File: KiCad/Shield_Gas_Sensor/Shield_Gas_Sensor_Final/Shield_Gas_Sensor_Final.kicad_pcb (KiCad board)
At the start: 2 copper layers, 68.6 x 53.3 mm, 20 parts, among them P1 Power, P2 Analog, P3 Digital, P4 Digital, P5 CONN_01X01, P6 CONN_01X01, P7 CONN_01X01, P8 CONN_01X01, U1 LTC1050ACN8#PBF, U2 Gas_Sensor_TO-5, U3 RN2483_Breakout

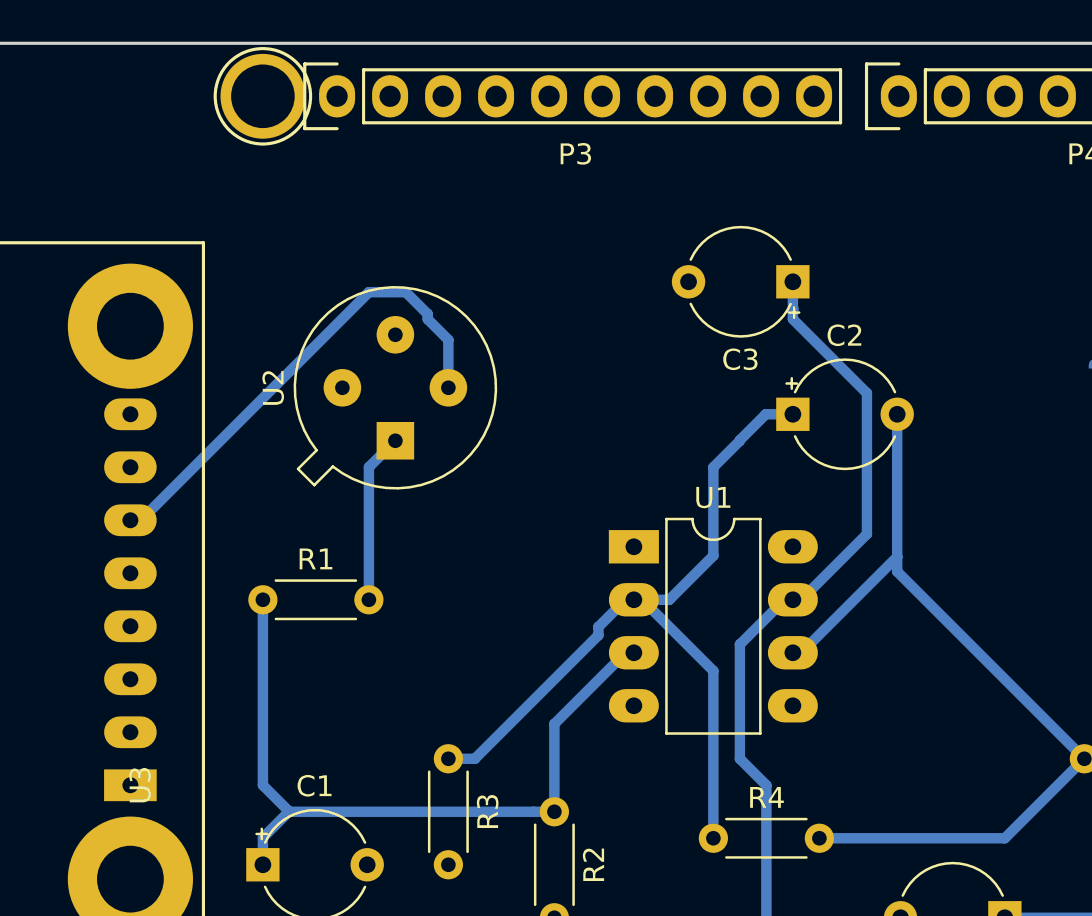
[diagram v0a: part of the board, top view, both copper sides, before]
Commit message: Correction Tx/Rx and Screens
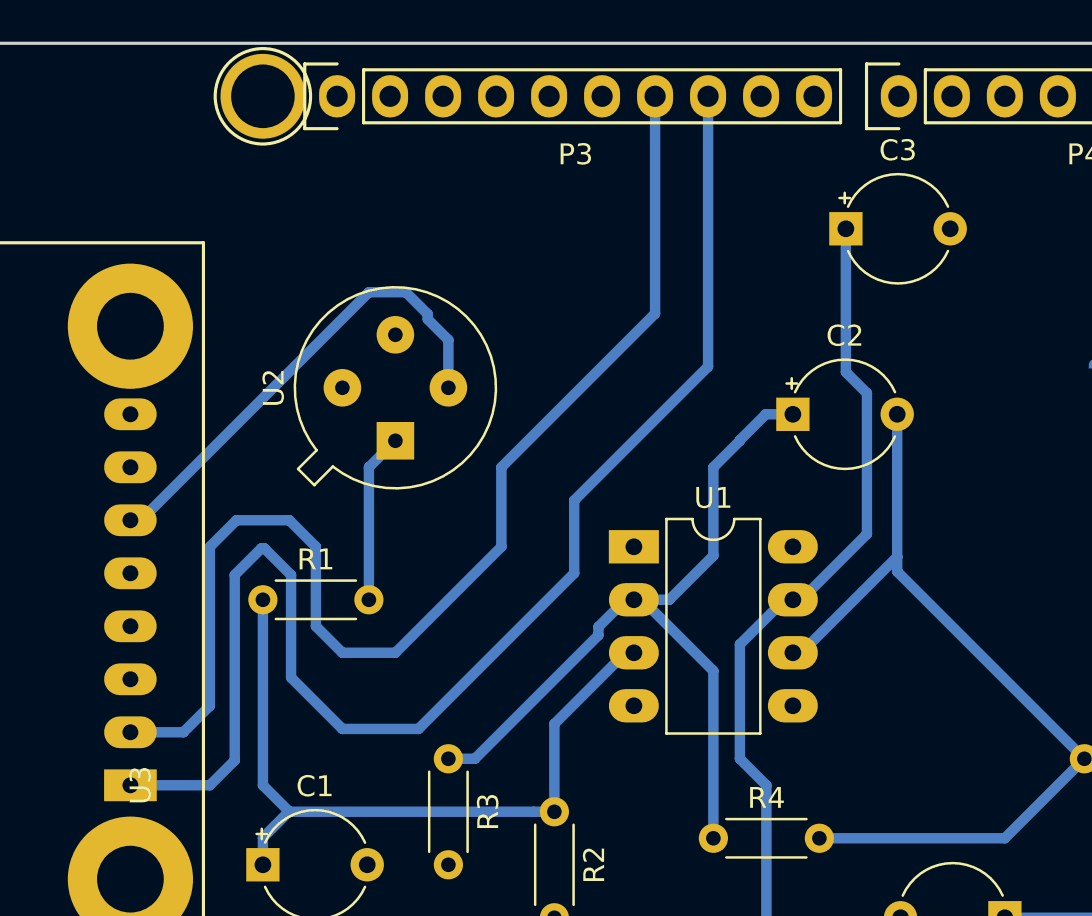
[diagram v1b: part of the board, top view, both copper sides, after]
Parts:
- moved C3 3.59 mm to (154.2, 81.9), turned to 0 degrees
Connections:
- U3 pad 1: /10 -> /10(**/SS)
- U3 pad 2: /11 -> /11(**/MOSI)
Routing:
- net /10(**/SS): track 0.00 -> 66.3 mm
- net /11(**/MOSI): track 0.00 -> 58.1 mm
- net +5V: track 44.9 -> 46.4 mm
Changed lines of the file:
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@@
     (thickness 1.6)
     (drawings 28)
-    (tracks 59)
+    (tracks 83)
     (zones 0)
     (modules 20)
-    (nets 49)
+    (nets 47)
   )
   (page A4)
@@
   (net 41 "Net-(U2-Pad3)")
   (net 42 "Net-(U2-Pad4)")
-  (net 43 /10)
-  (net 44 /11)
-  (net 45 "Net-(U3-Pad3)")
-  (net 46 "Net-(U3-Pad4)")
-  (net 47 "Net-(U3-Pad5)")
-  (net 48 "Net-(U3-Pad7)")
+  (net 43 "Net-(U3-Pad3)")
+  (net 44 "Net-(U3-Pad4)")
+  (net 45 "Net-(U3-Pad5)")
+  (net 46 "Net-(U3-Pad7)")
   (net_class Default "This is the default net class."
     (clearance 0.4)
@@
     (add_net "/0(Rx)")
     (add_net "/1(Tx)")
-    (add_net /10)
     (add_net "/10(**/SS)")
-    (add_net /11)
     (add_net "/11(**/MOSI)")
     (add_net "/12(MISO)")
@@
   )
   (module Capacitor_THT:CP_Radial_Tantal_D5.0mm_P5.00mm (layer F.Cu)
-    (at 151.638 84.455 180)
+    (at 154.178 81.915)
     (descr "CP, Radial_Tantal series, Radial, pin pitch=5.00mm, , diameter=5.0mm, Tantal Electrolytic Capacitor, http://cdn-reichelt.de/documents/datenblatt/B300/TANTAL-TB-Serie%23.pdf")
     (tags "CP Radial_Tantal series Radial pin pitch 5.00mm  diameter 5.0mm Tantal Electrolytic Capacitor")
-    (fp_text reference C3 (at 2.5 -3.75 180) (layer F.SilkS)
-      (effects (font (size 1 1) (thickness 0.15)))
-    )
-    (fp_text value 100n (at 2.5 3.75 180) (layer F.Fab)
-      (effects (font (size 1 1) (thickness 0.15)))
-    )
-    (fp_text user %R (at 2.54 0 180) (layer F.Fab)
+    (fp_text reference C3 (at 2.5 -3.75) (layer F.SilkS)
+      (effects (font (size 1 1) (thickness 0.15)))
+    )
+    (fp_text value 100n (at 2.5 3.75) (layer F.Fab)
+      (effects (font (size 1 1) (thickness 0.15)))
+    )
+    (fp_text user %R (at 2.54 0) (layer F.Fab)
       (effects (font (size 1 1) (thickness 0.15)))
     )
@@
     (fp_arc (start 2.5 0) (end 0.104003 1.06) (angle -132.27036) (layer F.SilkS) (width 0.12))
     (fp_arc (start 2.5 0) (end 0.104003 -1.06) (angle 132.27036) (layer F.SilkS) (width 0.12))
-    (pad 2 thru_hole circle (at 5 0 180) (size 1.6 1.6) (drill 0.8) (layers *.Cu *.Mask)
+    (pad 2 thru_hole circle (at 5 0) (size 1.6 1.6) (drill 0.8) (layers *.Cu *.Mask)
       (net 4 GND))
-    (pad 1 thru_hole rect (at 0 0 180) (size 1.6 1.6) (drill 0.8) (layers *.Cu *.Mask)
+    (pad 1 thru_hole rect (at 0 0) (size 1.6 1.6) (drill 0.8) (layers *.Cu *.Mask)
       (net 3 +5V))
     (model ${KISYS3DMOD}/Capacitor_THT.3dshapes/CP_Radial_Tantal_D5.0mm_P5.00mm.wrl
@@
     (fp_line (start -8 -46.5) (end -8 3.5) (layer F.SilkS) (width 0.15))
     (pad 1 thru_hole rect (at 0 0 90) (size 1.524 2.524) (drill 0.762) (layers *.Cu *.Mask)
-      (net 43 /10))
+      (net 28 "/10(**/SS)"))
     (pad 2 thru_hole oval (at 2.54 0 90) (size 1.524 2.524) (drill 0.762) (layers *.Cu *.Mask)
-      (net 44 /11))
+      (net 32 "/11(**/MOSI)"))
     (pad 3 thru_hole oval (at 5.08 0 90) (size 1.524 2.524) (drill 0.762) (layers *.Cu *.Mask)
-      (net 45 "Net-(U3-Pad3)"))
+      (net 43 "Net-(U3-Pad3)"))
     (pad 4 thru_hole oval (at 7.62 0 90) (size 1.524 2.524) (drill 0.762) (layers *.Cu *.Mask)
-      (net 46 "Net-(U3-Pad4)"))
+      (net 44 "Net-(U3-Pad4)"))
     (pad 5 thru_hole oval (at 10.16 0 90) (size 1.524 2.524) (drill 0.762) (layers *.Cu *.Mask)
-      (net 47 "Net-(U3-Pad5)"))
+      (net 45 "Net-(U3-Pad5)"))
     (pad 6 thru_hole oval (at 12.7 0 90) (size 1.524 2.524) (drill 0.762) (layers *.Cu *.Mask)
       (net 40 /3V3))
     (pad 7 thru_hole oval (at 15.24 0 90) (size 1.524 2.524) (drill 0.762) (layers *.Cu *.Mask)
-      (net 48 "Net-(U3-Pad7)"))
+      (net 46 "Net-(U3-Pad7)"))
     (pad 8 thru_hole oval (at 17.78 0 90) (size 1.524 2.524) (drill 0.762) (layers *.Cu *.Mask)
       (net 4 GND))
@@
   (segment (start 149.098 107.315) (end 149.098 101.835) (width 0.5) (layer B.Cu) (net 3))
   (segment (start 152.038 99.695) (end 151.638 99.695) (width 0.5) (layer B.Cu) (net 3))
-  (segment (start 151.638 84.455) (end 151.638 85.755) (width 0.5) (layer B.Cu) (net 3))
-  (segment (start 151.638 85.755) (end 151.668 85.755) (width 0.5) (layer B.Cu) (net 3))
   (segment (start 155.187999 89.795001) (end 155.187999 96.545001) (width 0.5) (layer B.Cu) (net 3))
   (segment (start 155.187999 96.545001) (end 152.038 99.695) (width 0.5) (layer B.Cu) (net 3))
-  (segment (start 151.638 86.245002) (end 155.187999 89.795001) (width 0.5) (layer B.Cu) (net 3))
-  (segment (start 151.638 85.755) (end 151.638 86.245002) (width 0.5) (layer B.Cu) (net 3))
+  (segment (start 154.178 88.785002) (end 154.178 81.915) (width 0.5) (layer B.Cu) (net 3))
+  (segment (start 154.178 88.785002) (end 155.187999 89.795001) (width 0.5) (layer B.Cu) (net 3))
   (segment (start 161.798 114.935) (end 161.798 123.825) (width 0.5) (layer B.Cu) (net 6))
   (segment (start 161.798 114.935) (end 166.878 114.935) (width 0.5) (layer B.Cu) (net 6))
   (segment (start 170.688 111.125) (end 170.688 107.315) (width 0.5) (layer B.Cu) (net 6))
   (segment (start 166.878 114.935) (end 170.688 111.125) (width 0.5) (layer B.Cu) (net 6))
+  (segment (start 133.697998 105.884998) (end 141.157996 98.425) (width 0.5) (layer B.Cu) (net 28))
+  (segment (start 130.048 105.884998) (end 133.697998 105.884998) (width 0.5) (layer B.Cu) (net 28))
+  (segment (start 127.588001 98.505001) (end 127.588001 103.424999) (width 0.5) (layer B.Cu) (net 28))
+  (segment (start 141.157996 98.425) (end 141.157996 94.935004) (width 0.5) (layer B.Cu) (net 28))
+  (segment (start 123.698 108.585) (end 124.887999 107.395001) (width 0.5) (layer B.Cu) (net 28))
+  (segment (start 147.574 88.519) (end 147.574 75.565) (width 0.5) (layer B.Cu) (net 28))
+  (segment (start 119.888 108.585) (end 123.698 108.585) (width 0.5) (layer B.Cu) (net 28))
+  (segment (start 124.887999 107.395001) (end 124.887999 98.505001) (width 0.5) (layer B.Cu) (net 28))
+  (segment (start 141.157996 94.935004) (end 147.574 88.519) (width 0.5) (layer B.Cu) (net 28))
+  (segment (start 127.588001 103.424999) (end 130.048 105.884998) (width 0.5) (layer B.Cu) (net 28))
+  (segment (start 124.887999 98.505001) (end 126.157999 97.235001) (width 0.5) (layer B.Cu) (net 28))
+  (segment (start 126.157999 97.235001) (end 126.318001 97.235001) (width 0.5) (layer B.Cu) (net 28))
+  (segment (start 126.318001 97.235001) (end 127.588001 98.505001) (width 0.5) (layer B.Cu) (net 28))
+  (segment (start 145.034 85.979) (end 145.034 75.565) (width 0.5) (layer B.Cu) (net 32))
+  (segment (start 137.668 97.155) (end 137.668 93.345) (width 0.5) (layer B.Cu) (net 32))
+  (segment (start 132.588 102.235) (end 137.668 97.155) (width 0.5) (layer B.Cu) (net 32))
+  (segment (start 130.048 102.235) (end 132.588 102.235) (width 0.5) (layer B.Cu) (net 32))
+  (segment (start 128.778 100.965) (end 130.048 102.235) (width 0.5) (layer B.Cu) (net 32))
+  (segment (start 137.668 93.345) (end 145.034 85.979) (width 0.5) (layer B.Cu) (net 32))
+  (segment (start 122.428 106.045) (end 123.698 104.775) (width 0.5) (layer B.Cu) (net 32))
+  (segment (start 128.778 97.155) (end 128.778 100.965) (width 0.5) (layer B.Cu) (net 32))
+  (segment (start 119.888 106.045) (end 122.428 106.045) (width 0.5) (layer B.Cu) (net 32))
+  (segment (start 123.698 104.775) (end 123.698 97.155) (width 0.5) (layer B.Cu) (net 32))
+  (segment (start 123.698 97.155) (end 124.968 95.885) (width 0.5) (layer B.Cu) (net 32))
+  (segment (start 124.968 95.885) (end 127.508 95.885) (width 0.5) (layer B.Cu) (net 32))
+  (segment (start 127.508 95.885) (end 128.778 97.155) (width 0.5) (layer B.Cu) (net 32))
   (segment (start 139.218051 109.855) (end 140.208 109.855) (width 0.5) (layer B.Cu) (net 33))
   (segment (start 126.238 111.095) (end 127.478 109.855) (width 0.5) (layer B.Cu) (net 33))
